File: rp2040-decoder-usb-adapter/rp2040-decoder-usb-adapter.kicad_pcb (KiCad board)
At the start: 2 copper layers, 42 x 16.8 mm, 13 parts, among them J1 505070-2422, J2 SWD, J3 SPEAKER, J4 MISC1, J8 RAIL_PADS, P1 USB_C_Receptacle_USB2.0_16P

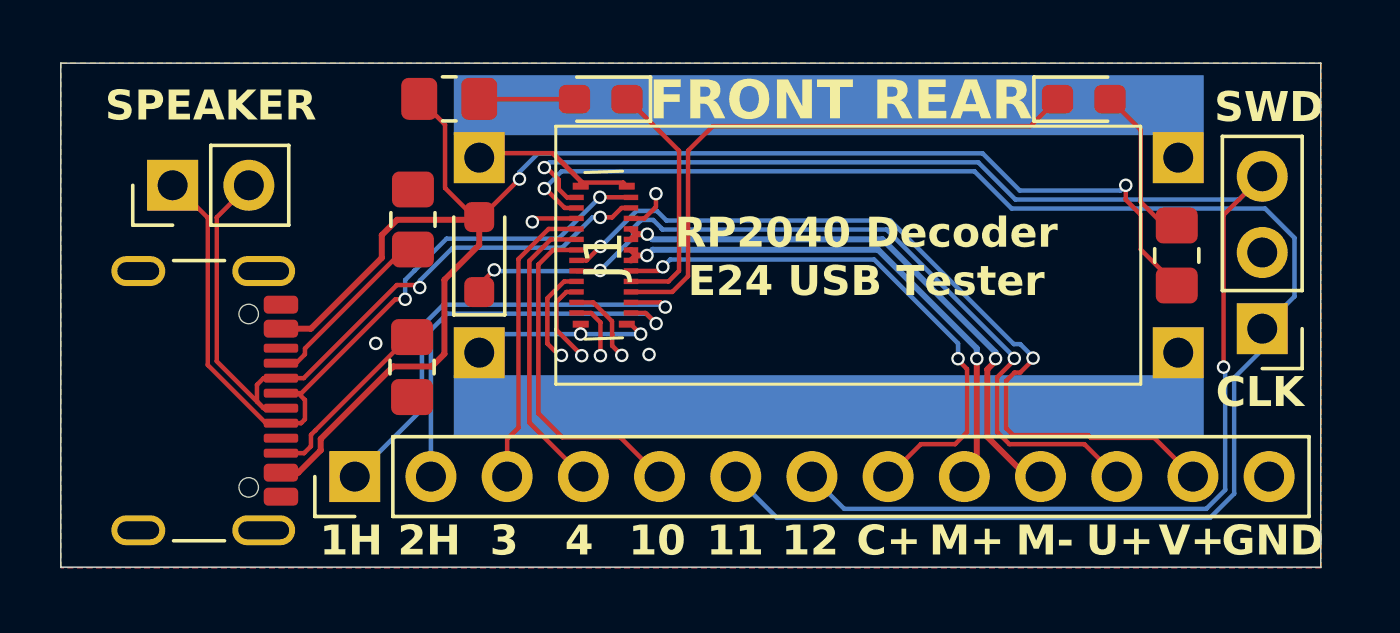
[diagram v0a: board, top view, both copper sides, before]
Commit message: feat: add external capacitor support
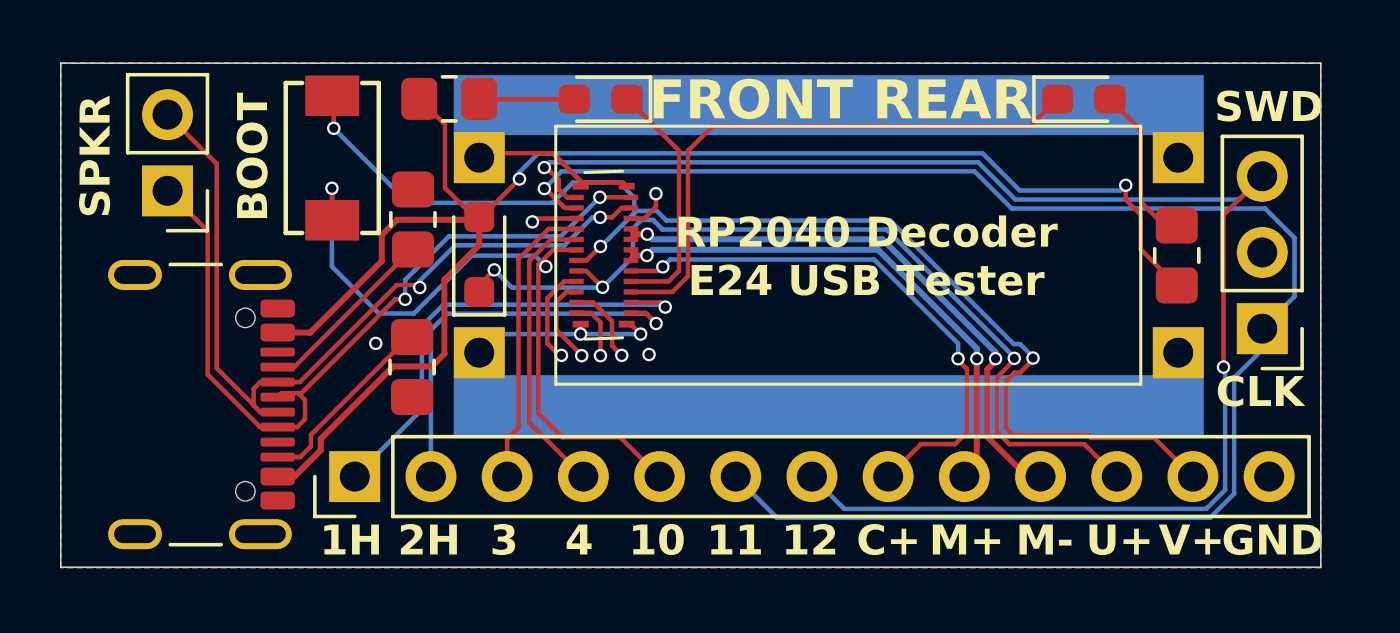
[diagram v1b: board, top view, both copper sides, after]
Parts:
- added SW1: BOOT, Local Library:Xunpu_TS-1088-AR02016, F.Cu at (148.8, 78.7)
- moved J3 0.25 mm to (143.4, 79.8), turned to 180 degrees
- moved P1 0.17 mm to (143.3, 86.9)
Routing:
- net VCC: track 27.7 -> 40.9 mm, vias 2 -> 3
- net /AUX10: track 11.3 -> 23.8 mm, vias 0 -> 2
- net /D-: track 25.7 -> 28.5 mm
- net VDC: track 29.3 -> 30.3 mm
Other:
- board text added: "BOOT"
- board text added: "SPKR"
- board text removed: "SPEAKER"

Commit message: fix: make boot button easier to press
fix: dfm fixes
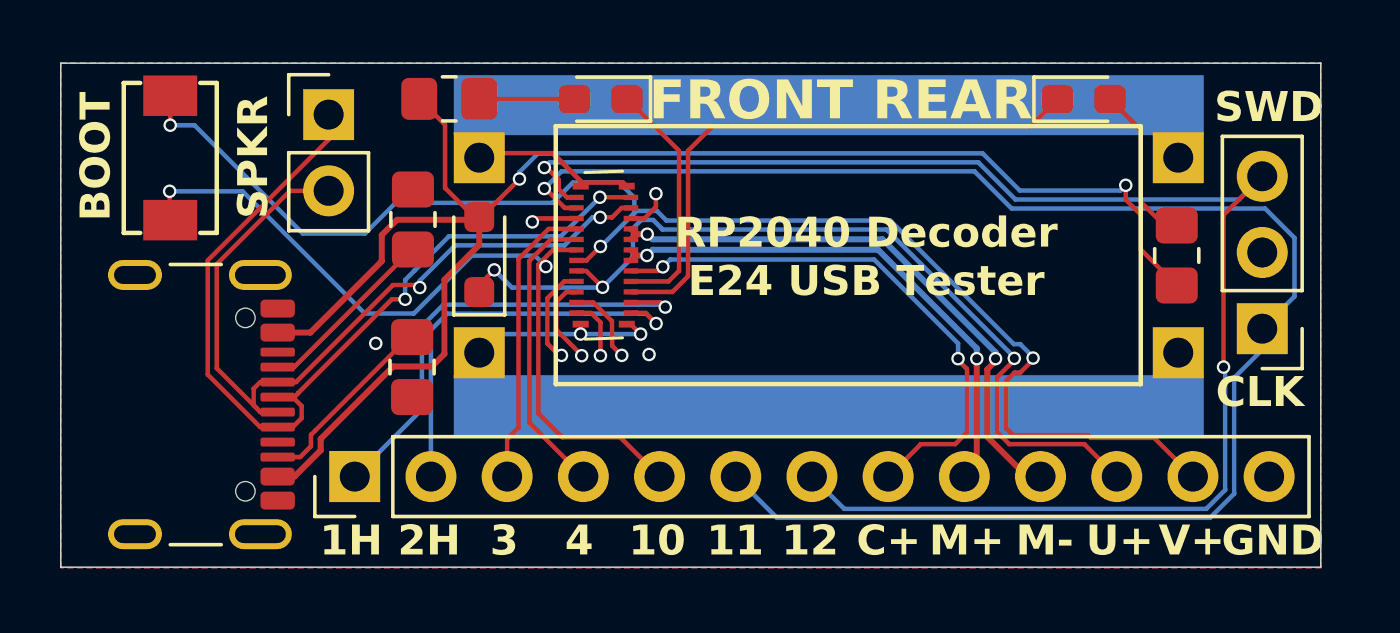
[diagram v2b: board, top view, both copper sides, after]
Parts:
- moved J3 5.94 mm to (148.7, 77.3), turned to 0 degrees
- moved SW1 5.40 mm to (143.4, 78.7)
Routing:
- net VCC: track 40.9 -> 47.1 mm
- net /D+: track 26.6 -> 30.6 mm
- net /AUX10: track 23.8 -> 27.5 mm
- net /D-: track 28.5 -> 27.6 mm

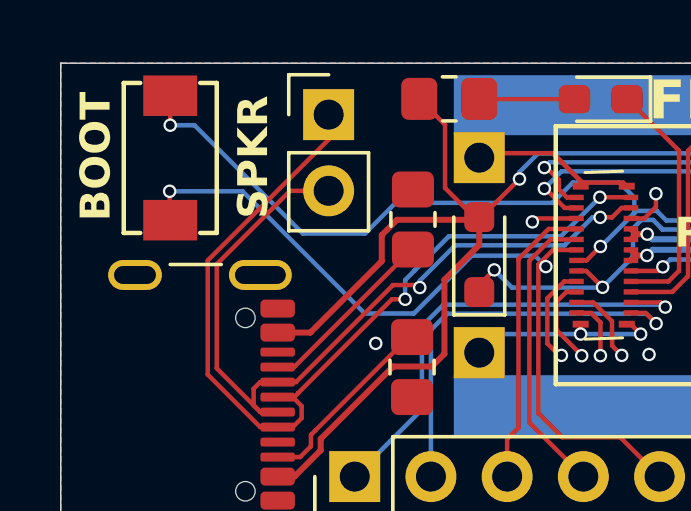
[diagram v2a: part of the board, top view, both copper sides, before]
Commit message: fix: switch button type
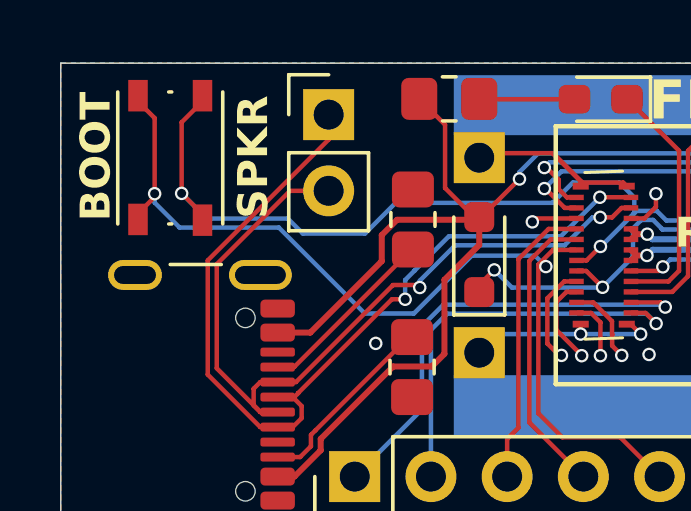
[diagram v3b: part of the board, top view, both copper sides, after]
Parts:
- SW1: footprint Local Library:Xunpu_TS-1088-AR02016 -> Button_Switch_SMD:SW_Push_1P1T_NO_Vertical_Wuerth_434133025816
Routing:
- net /AUX10: track 27.5 -> 31.8 mm
- net VCC: track 47.1 -> 49.5 mm
